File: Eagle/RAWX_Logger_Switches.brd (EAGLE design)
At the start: 25.4 x 22.9 mm, 11 parts

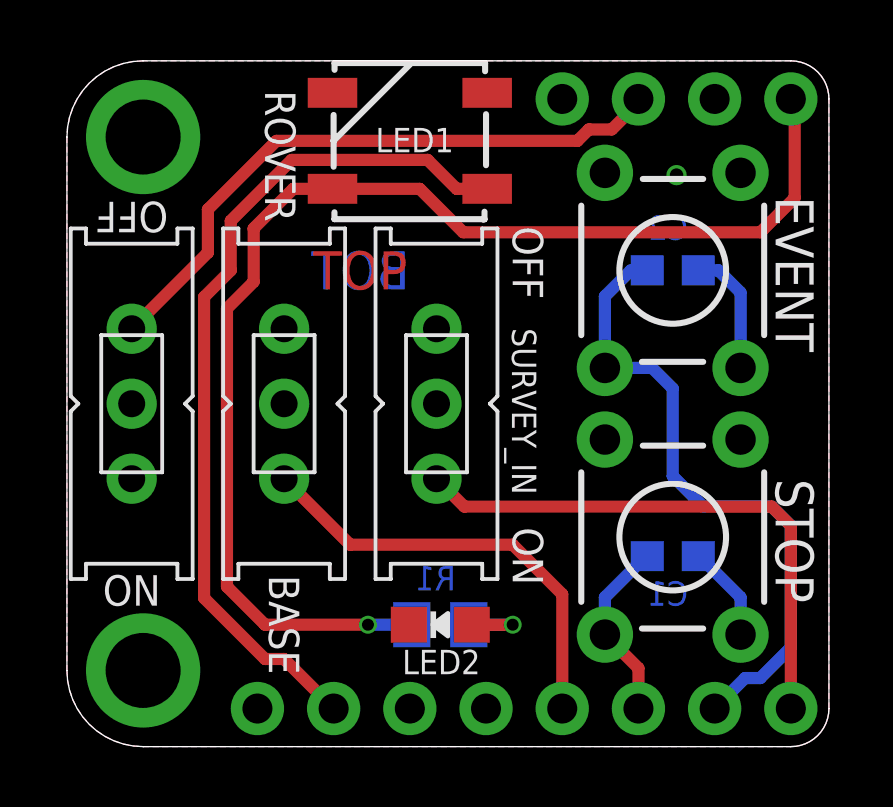
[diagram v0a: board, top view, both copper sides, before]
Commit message: Updated the switch positions
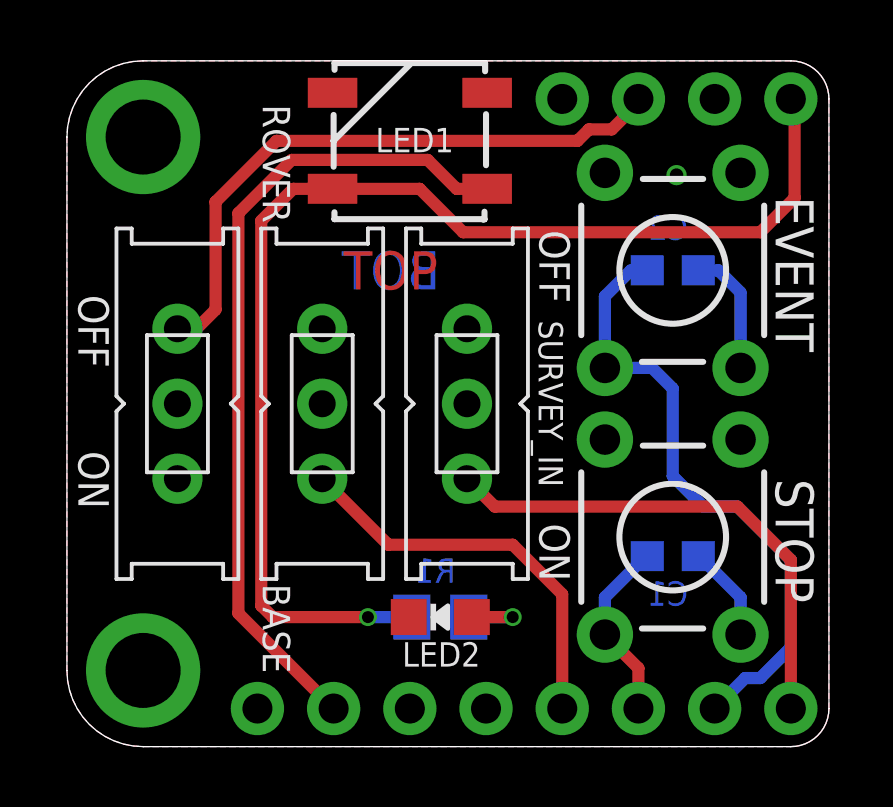
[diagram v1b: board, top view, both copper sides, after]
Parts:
- moved S1 1.52 mm to (3.68, 11.4)
- moved BASE 1.27 mm to (8.51, 11.4)
- moved SURVEY_IN 1.02 mm to (13.3, 11.4)
- moved LED2 0.25 mm to (12.4, 4.32)
- moved R1 0.25 mm to (12.4, 4.32)
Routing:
- net SURVEY_IN: track 18.6 -> 16.9 mm
- net GPIO13: track 42.0 -> 40.7 mm
- net 3V: track 28.6 -> 27.3 mm
- net BASE: track 14.7 -> 13.4 mm
- net EVENT: track 21.7 -> 21.0 mm
